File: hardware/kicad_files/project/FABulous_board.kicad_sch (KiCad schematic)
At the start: 7 parts, among them SW1 Tactile Switch

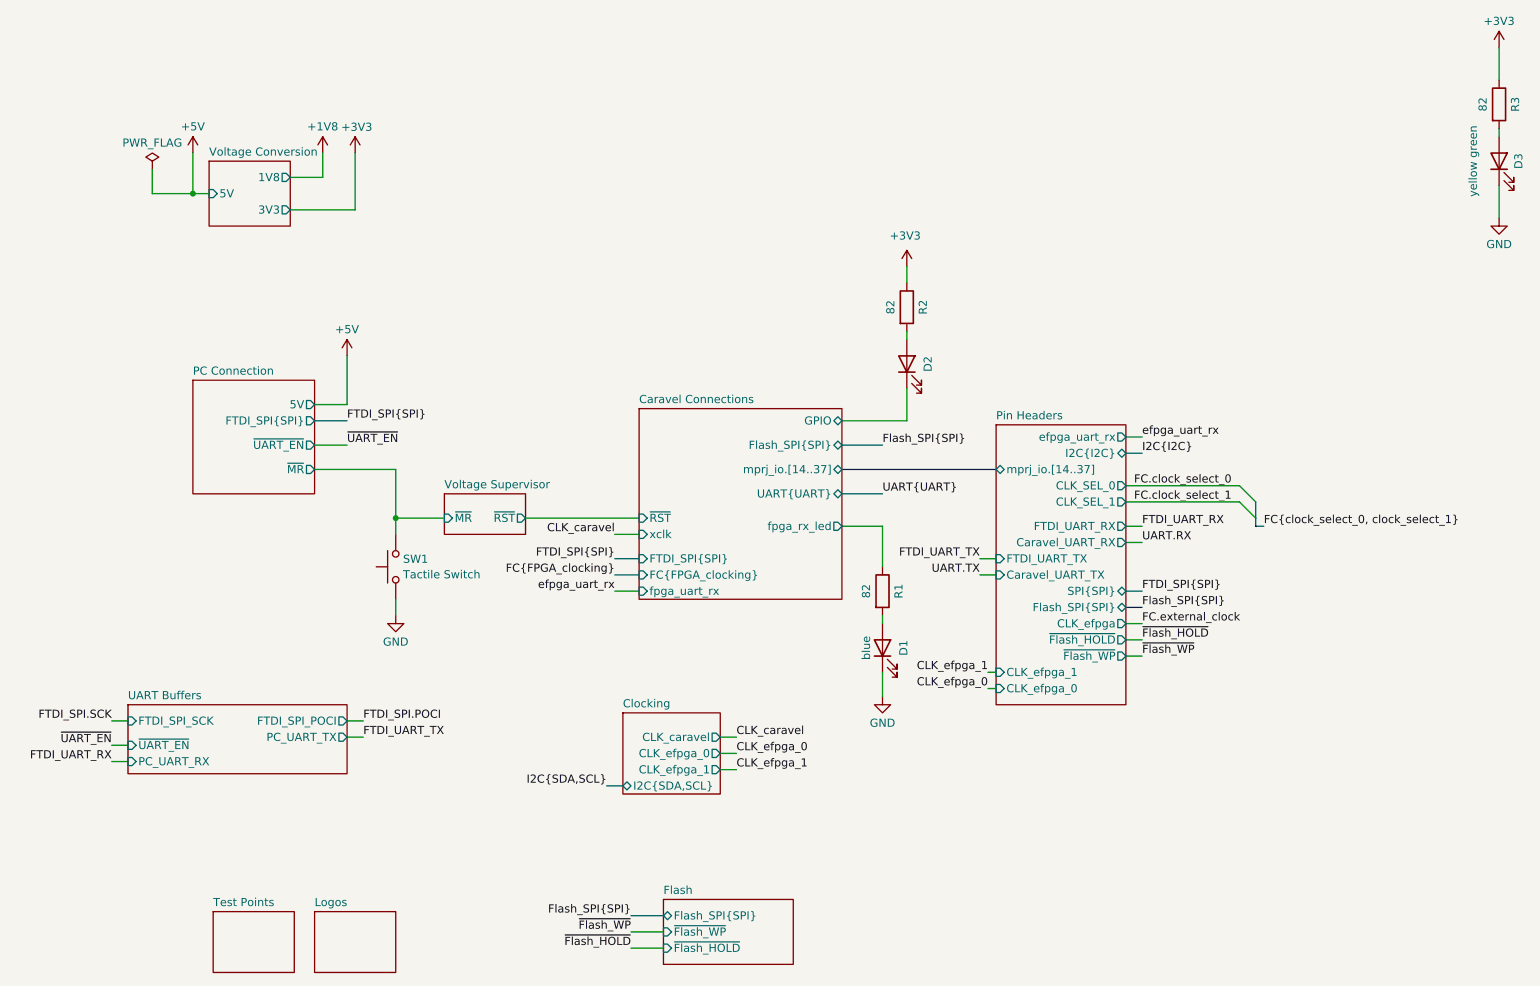
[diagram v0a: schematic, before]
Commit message: feat: update to 0.2
feat: add pin sockets compatible to the Pmod interface

feat: add a power switch and an overcurrent protection circuit, including a fault status LED and a solder bridge

fix: remove the clock jumpers and directly connect the second output clock to the user clock input

misc: remove the jumpers from io 36 and 37 to the bitbang inputs, add bitbang pins to the UART connector

cosmetic: make the PCB edges round
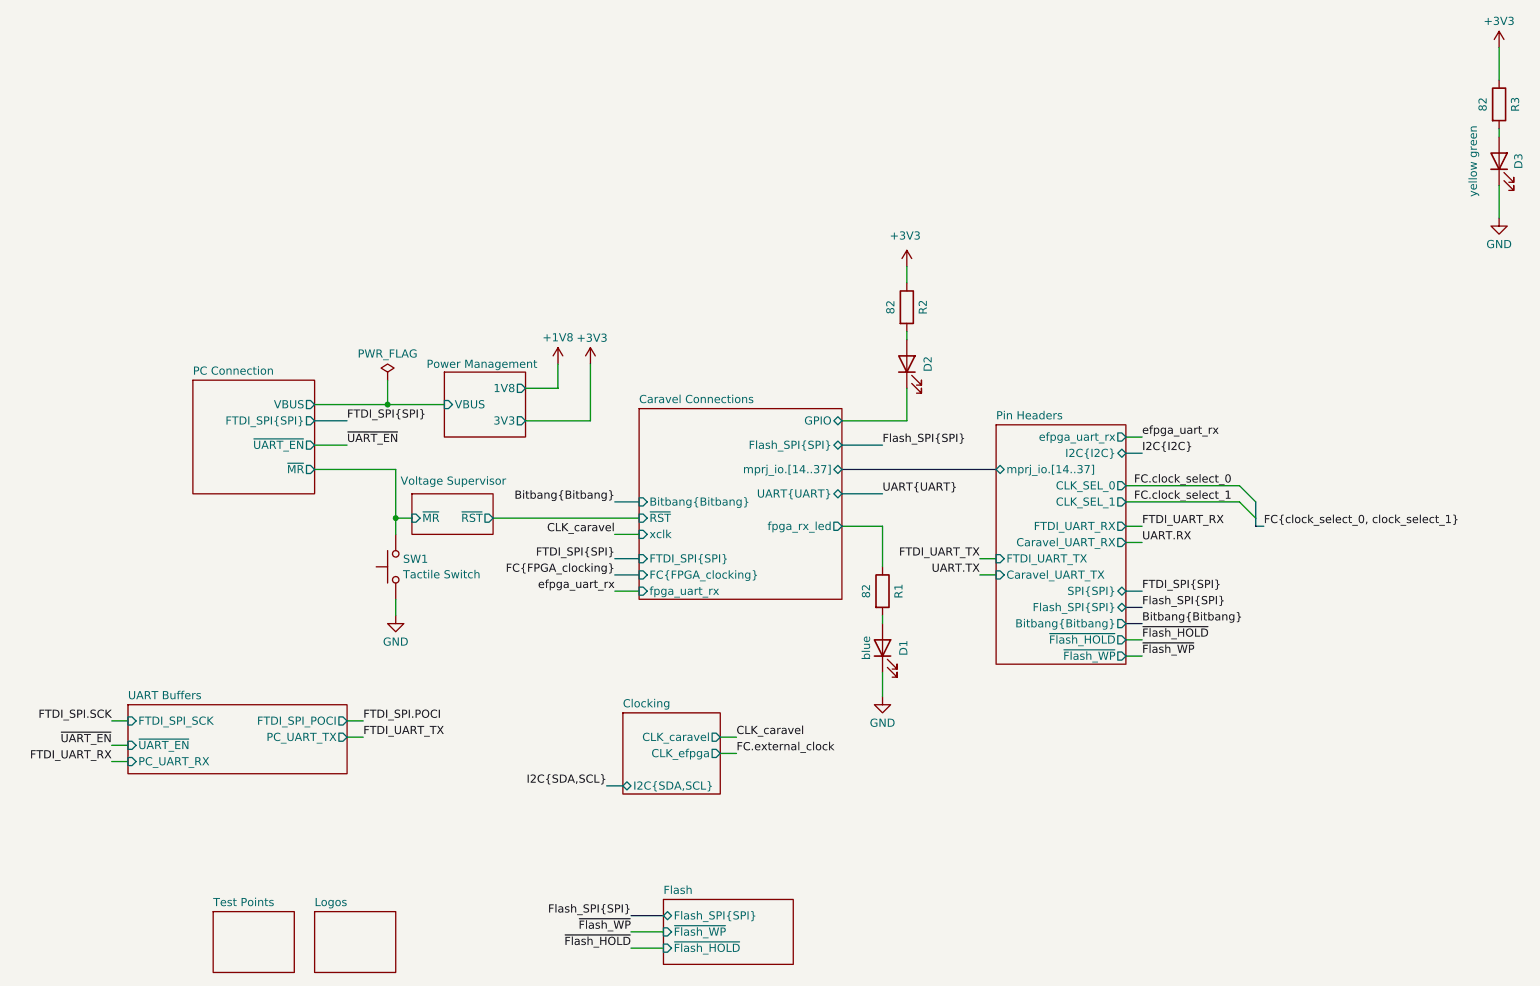
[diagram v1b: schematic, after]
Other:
- sheet Voltage Conversion renamed Power Management
- sheet Caravel Connections ports: added Bitbang{Bitbang}; removed none
- sheet Clocking ports: added CLK_efpga; removed CLK_efpga_0, CLK_efpga_1
- sheet PC Connection ports: added VBUS; removed 5V
- sheet Pin Headers ports: added Bitbang{Bitbang}; removed CLK_efpga, CLK_efpga_0, CLK_efpga_1
- sheet Power Management ports: added VBUS; removed 5V
